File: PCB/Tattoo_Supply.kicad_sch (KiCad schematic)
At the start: 1 part

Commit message: ok stm32
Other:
- sheet MCU ports: added Analog1, Analog2, Display{SPI}, I2C{I2C}, SW1, SW2, USB{USB2}, V_{IN}; removed none

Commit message: ok mcu
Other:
- sheet MCU ports: added none; removed Display{SPI}
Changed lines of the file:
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@@
   (bus_alias "SPI" (members "~{CS}" "SCK" "MOSI" "MISO"))
   (bus_alias "I2C" (members "SDA" "SCL"))
+  (bus_alias "Encoder" (members "DT" "CLK" "SW"))
   (bus_alias "USB2" (members "D+" "D-"))
+  (bus_alias "UART" (members "Tx" "Rx"))
   (symbol (lib_id "Connector:Jack-DC") (at 54.61 91.44 0) (unit 1)
     (in_bom yes) (on_board yes) (fields_autoplaced)
@@
       (effects (font (size 1.27 1.27)) (justify left top))
     )
-    (pin "Display{SPI}" bidirectional (at 165.1 101.6 0)
-      (effects (font (size 1.27 1.27)) (justify right))
-    )
     (pin "Analog1" input (at 165.1 111.76 0)
       (effects (font (size 1.27 1.27)) (justify right))
@@
       (reference "#PWR?") (unit 1) (value "GND") (footprint "")
     )
+    (path "/ceea0ffd-34e8-4863-a5ab-807ee81bbc9d/209d5f48-9dee-4bd0-b02d-227aeb5c4318"
+      (reference "#PWR?") (unit 1) (value "GND") (footprint "")
+    )
     (path "/fd65dc63-1d27-4821-ae4f-326fe3a44815/219d7a54-ba85-401f-8dc0-d54a54827849"
       (reference "#PWR?") (unit 1) (value "GND") (footprint "")
@@
       (reference "#PWR?") (unit 1) (value "GND") (footprint "")
     )
+    (path "/ceea0ffd-34e8-4863-a5ab-807ee81bbc9d/6e2f87e8-4322-4c83-993d-abf7d7702da7"
+      (reference "#PWR?") (unit 1) (value "GND") (footprint "")
+    )
     (path "/fd65dc63-1d27-4821-ae4f-326fe3a44815/70e931da-5280-4fcb-8adb-62962b0bf36b"
       (reference "#PWR?") (unit 1) (value "GND") (footprint "")
     )
+    (path "/ceea0ffd-34e8-4863-a5ab-807ee81bbc9d/739a57d0-cd48-4cfe-b3e1-84199a8baf62"
+      (reference "#PWR?") (unit 1) (value "GND") (footprint "")
+    )
+    (path "/ceea0ffd-34e8-4863-a5ab-807ee81bbc9d/92e2621e-1d94-4672-aa9c-724bd8707c89"
+      (reference "#PWR?") (unit 1) (value "GND") (footprint "")
+    )
     (path "/fd65dc63-1d27-4821-ae4f-326fe3a44815/a8618119-4c0b-4959-bbf1-46448de5cd11"
       (reference "#PWR?") (unit 1) (value "GND") (footprint "")
     )
+    (path "/ceea0ffd-34e8-4863-a5ab-807ee81bbc9d/b1d808bc-dda0-4732-8ccc-96778c209527"
+      (reference "#PWR?") (unit 1) (value "GND") (footprint "")
+    )
+    (path "/fd65dc63-1d27-4821-ae4f-326fe3a44815/cb70f95d-98c3-4234-976a-6d0b037f67cd"
+      (reference "#PWR?") (unit 1) (value "GND") (footprint "")
+    )
     (path "/fd65dc63-1d27-4821-ae4f-326fe3a44815/ce2cea56-afbe-4c0c-9152-4809b0e243ab"
+      (reference "#PWR?") (unit 1) (value "GND") (footprint "")
+    )
+    (path "/fd65dc63-1d27-4821-ae4f-326fe3a44815/d3881261-65ae-4324-a13e-0bd2ac652f6b"
+      (reference "#PWR?") (unit 1) (value "GND") (footprint "")
+    )
+    (path "/fd65dc63-1d27-4821-ae4f-326fe3a44815/dec39829-4ba5-4851-9fe3-ab379efdf29e"
       (reference "#PWR?") (unit 1) (value "GND") (footprint "")
     )
@@
       (reference "C?") (unit 1) (value "100n") (footprint "")
     )
+    (path "/fd65dc63-1d27-4821-ae4f-326fe3a44815/3f28275f-fa59-40af-b9ba-f1db5b1bffba"
+      (reference "C?") (unit 1) (value "100n") (footprint "")
+    )
+    (path "/fd65dc63-1d27-4821-ae4f-326fe3a44815/426923ec-93c5-45de-a0b2-8377a0d1b5b5"
+      (reference "C?") (unit 1) (value "100n") (footprint "")
+    )
     (path "/fd65dc63-1d27-4821-ae4f-326fe3a44815/50a776f3-c84e-45f3-bdc5-88ccb16d4fa8"
       (reference "C?") (unit 1) (value "10n") (footprint "")
     )
+    (path "/ceea0ffd-34e8-4863-a5ab-807ee81bbc9d/59aca0d5-fb73-446c-8044-31b5ea1b27e3"
+      (reference "C?") (unit 1) (value "100u") (footprint "")
+    )
     (path "/fd65dc63-1d27-4821-ae4f-326fe3a44815/63fc3922-5575-4797-a8b4-026434bbdba2"
       (reference "C?") (unit 1) (value "20p") (footprint "")
@@
       (reference "C?") (unit 1) (value "100n") (footprint "")
     )
+    (path "/ceea0ffd-34e8-4863-a5ab-807ee81bbc9d/c91fc11c-ab73-413f-9ad8-e9aebe7918a4"
+      (reference "C?") (unit 1) (value "C_Polarized") (footprint "")
+    )
+    (path "/fd65dc63-1d27-4821-ae4f-326fe3a44815/f0dc52c5-f269-4d09-a7b2-26fb46b43ef8"
+      (reference "C?") (unit 1) (value "100n") (footprint "")
+    )
     (path "/fd65dc63-1d27-4821-ae4f-326fe3a44815/f390d7db-f656-449d-9645-869edcae1d7d"
       (reference "C?") (unit 1) (value "100n") (footprint "")
+    )
+    (path "/ceea0ffd-34e8-4863-a5ab-807ee81bbc9d/542b5997-5523-4b73-a962-b550c1a2d61d"
+      (reference "D?") (unit 1) (value "D_Schottky") (footprint "")
     )
     (path "/fd65dc63-1d27-4821-ae4f-326fe3a44815/d670595f-34bd-4ceb-bf89-2138a4aee6df"
       (reference "FB?") (unit 1) (value "FerriteBead") (footprint "")
     )
-    (path "/fd65dc63-1d27-4821-ae4f-326fe3a44815/262287fd-976a-40e1-86ca-178ad1aed119"
-      (reference "J?") (unit 1) (value "Conn_ARM_JTAG_SWD_10") (footprint "")
+    (path "/fd65dc63-1d27-4821-ae4f-326fe3a44815/27ba92e4-7a19-439e-a836-8d5326c322ee"
+      (reference "J?") (unit 1) (value "Conn_ST_STDC14") (footprint "")
     )
     (path "/4c52be23-334a-4437-8a45-f2c312d3c240"
       (reference "J?") (unit 1) (value "Jack-DC") (footprint "")
     )
+    (path "/fd65dc63-1d27-4821-ae4f-326fe3a44815/84eab48c-016a-46d9-ae05-455933d33fcc"
+      (reference "J?") (unit 1) (value "Conn_01x03") (footprint "")
+    )
     (path "/fd65dc63-1d27-4821-ae4f-326fe3a44815/cd014257-ed87-4ce3-b71c-554579d8f66e"
       (reference "J?") (unit 1) (value "Conn_ARM_SWD_TagConnect_TC2030-NL") (footprint "Connector:Tag-Connect_TC2030-IDC-NL_2x03_P1.27mm_Vertical")
@@
       (reference "JP?") (unit 1) (value "Jumper_3_Open") (footprint "")
     )
+    (path "/ceea0ffd-34e8-4863-a5ab-807ee81bbc9d/80b6b717-6ddb-483c-9ccb-7af1ed6ced4f"
+      (reference "L?") (unit 1) (value "L") (footprint "")
+    )
     (path "/fd65dc63-1d27-4821-ae4f-326fe3a44815/8a816776-bec8-412a-9b39-f908cd654c90"
       (reference "NT?") (unit 1) (value "NetTie_2") (footprint "")
     )
-    (path "/fd65dc63-1d27-4821-ae4f-326fe3a44815/1682e0a3-5848-4ad0-a20e-ea1765071bd3"
+    (path "/fd65dc63-1d27-4821-ae4f-326fe3a44815/080573f6-96ee-4bc9-963c-0b0c3e02c8d3"
       (reference "R?") (unit 1) (value "10k") (footprint "")
+    )
+    (path "/ceea0ffd-34e8-4863-a5ab-807ee81bbc9d/0a870a79-4320-460f-afd7-5b8aa7b0105a"
+      (reference "R?") (unit 1) (value "R") (footprint "")
     )
     (path "/fd65dc63-1d27-4821-ae4f-326fe3a44815/26955c41-e7d9-4961-9392-497c6b906013"
       (reference "R?") (unit 1) (value "100k") (footprint "")
     )
+    (path "/ceea0ffd-34e8-4863-a5ab-807ee81bbc9d/36c6f7fa-62ee-4a9e-b28b-a99c104b8804"
+      (reference "R?") (unit 1) (value "R") (footprint "")
+    )
+    (path "/fd65dc63-1d27-4821-ae4f-326fe3a44815/4afe15cf-e0e5-4313-8eae-78b1b4f1bd7c"
+      (reference "R?") (unit 1) (value "10k") (footprint "")
+    )
     (path "/fd65dc63-1d27-4821-ae4f-326fe3a44815/5242f7b3-0ed7-4e53-864f-924abef19174"
-      (reference "R?") (unit 1) (value "R") (footprint "")
+      (reference "R?") (unit 1) (value "953") (footprint "")
     )
     (path "/fd65dc63-1d27-4821-ae4f-326fe3a44815/5a84389e-b200-4c48-ace9-f152915889a8"
       (reference "R?") (unit 1) (value "100k") (footprint "")
     )
+    (path "/ceea0ffd-34e8-4863-a5ab-807ee81bbc9d/69cdcc3a-71ff-4d22-b373-8d0bfabffda2"
+      (reference "R?") (unit 1) (value "R") (footprint "")
+    )
     (path "/fd65dc63-1d27-4821-ae4f-326fe3a44815/bcc3352c-a803-4a6a-832b-8cf68c9698e4"
       (reference "R?") (unit 1) (value "DNP") (footprint "")
@@
       (reference "R?") (unit 1) (value "100k") (footprint "")
     )
+    (path "/fd65dc63-1d27-4821-ae4f-326fe3a44815/c261365f-e3fa-4f5e-8812-ea9045ff7b11"
+      (reference "R?") (unit 1) (value "10k") (footprint "")
+    )
     (path "/fd65dc63-1d27-4821-ae4f-326fe3a44815/d738e868-360a-41d5-ada5-28e9c2691349"
       (reference "R?") (unit 1) (value "4.7k") (footprint "")
     )
+    (path "/fd65dc63-1d27-4821-ae4f-326fe3a44815/e7fa5f6d-1fe1-4d75-a296-daf3a3ea18c5"
+      (reference "R?") (unit 1) (value "20") (footprint "")
+    )
+    (path "/fd65dc63-1d27-4821-ae4f-326fe3a44815/fa449a82-c0db-414c-9142-2e1aec3df6db"
+      (reference "R?") (unit 1) (value "20") (footprint "")
+    )
     (path "/fd65dc63-1d27-4821-ae4f-326fe3a44815/b30241f8-2e90-4809-aaff-57a210f91fd1"
       (reference "SW?") (unit 1) (value "SW_Push") (footprint "")
     )
+    (path "/fd65dc63-1d27-4821-ae4f-326fe3a44815/c9d98b02-57d9-4173-bb9a-ccfcc1182925"
+      (reference "SW?") (unit 1) (value "RotaryEncoder_Switch") (footprint "")
+    )
+    (path "/ceea0ffd-34e8-4863-a5ab-807ee81bbc9d/3734a769-29a5-4aca-94e3-fcaa690a41b0"
+      (reference "U?") (unit 1) (value "LM2576S-ADJ") (footprint "Package_TO_SOT_SMD:TO-263-5_TabPin3")
+    )
+    (path "/53d1b181-b4e9-4f58-bcbd-a7e6cd4ea6ab/716ceb08-5dd2-4aff-a561-f26e4abc0ca4"
+      (reference "U?") (unit 1) (value "STUSB4500QTR") (footprint "Package_DFN_QFN:QFN-24-1EP_4x4mm_P0.5mm_EP2.7x2.7mm")
+    )
     (path "/fd65dc63-1d27-4821-ae4f-326fe3a44815/76fa1aaf-a82a-42a7-951b-856edd37e98c"
       (reference "U?") (unit 1) (value "STM32F103C8Tx") (footprint "Package_QFP:LQFP-48_7x7mm_P0.5mm")
     )
     (path "/fd65dc63-1d27-4821-ae4f-326fe3a44815/40e99cce-c708-4322-9876-f46fc7779b96"
-      (reference "Y?") (unit 1) (value "Crystal") (footprint "")
-    )
-  )
+      (reference "Y?") (unit 1) (value "ABM3B-8.000MHZ-B2-T") (footprint "Crystal:Crystal_SMD_Abracon_ABM3B-4Pin_5.0x3.2mm")
+    )
+  )

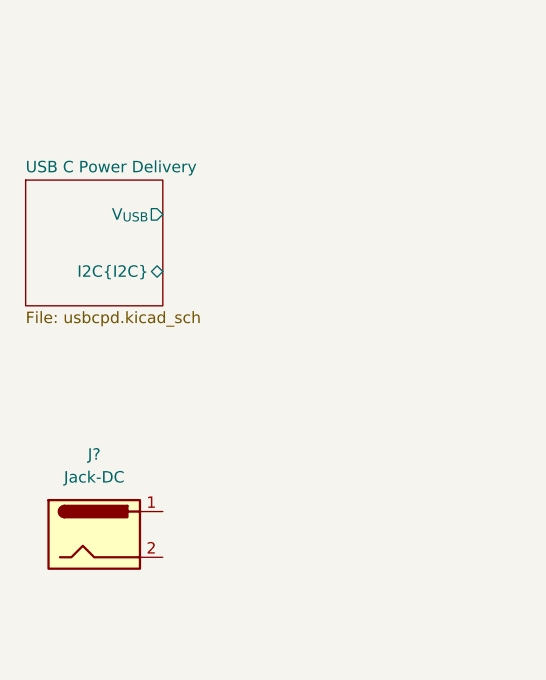
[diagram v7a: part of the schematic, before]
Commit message: upgrade usb protection + kicad 7
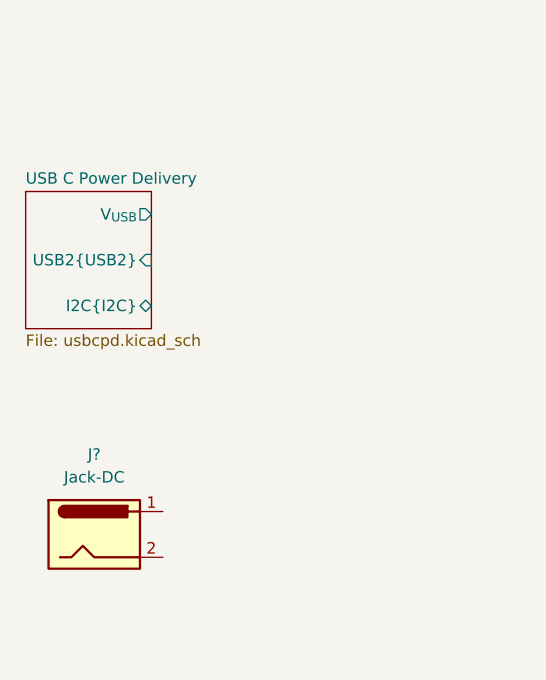
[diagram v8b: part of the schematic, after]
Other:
- sheet USB C Power Delivery ports: added USB2{USB2}; removed none
